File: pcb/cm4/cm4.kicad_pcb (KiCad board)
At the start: 4 copper layers, 100 x 80 mm, 30 parts, among them J101 Conn_02x10_Row_Letter_First, J201 DF40C-100DS-0.4V_51_, J202 DF40C-100DS-0.4V_51_, J301 HR911130A, U201 SN74LV1T34DBV, U301 TPD4EUSB30, U302 TPD4EUSB30, U401 RT9742GGJ5

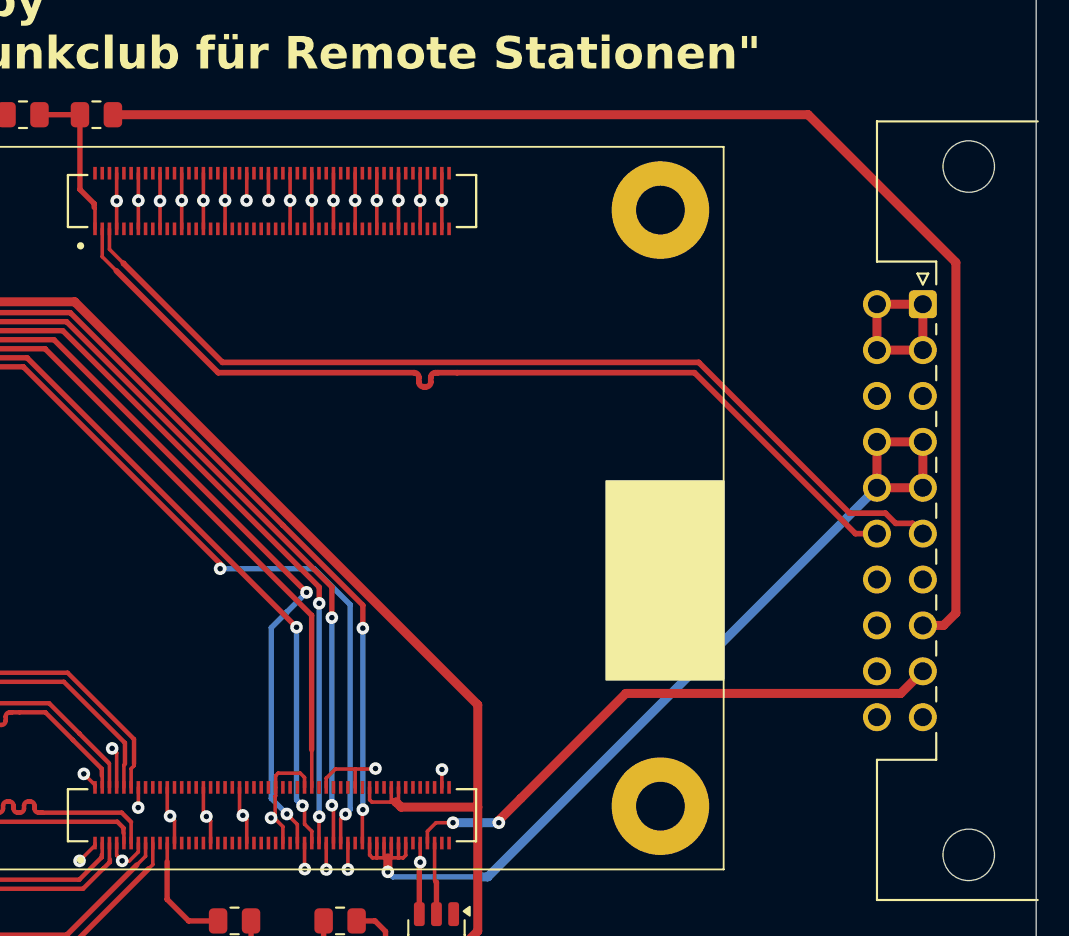
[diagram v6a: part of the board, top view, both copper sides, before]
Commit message: fix pin assignment
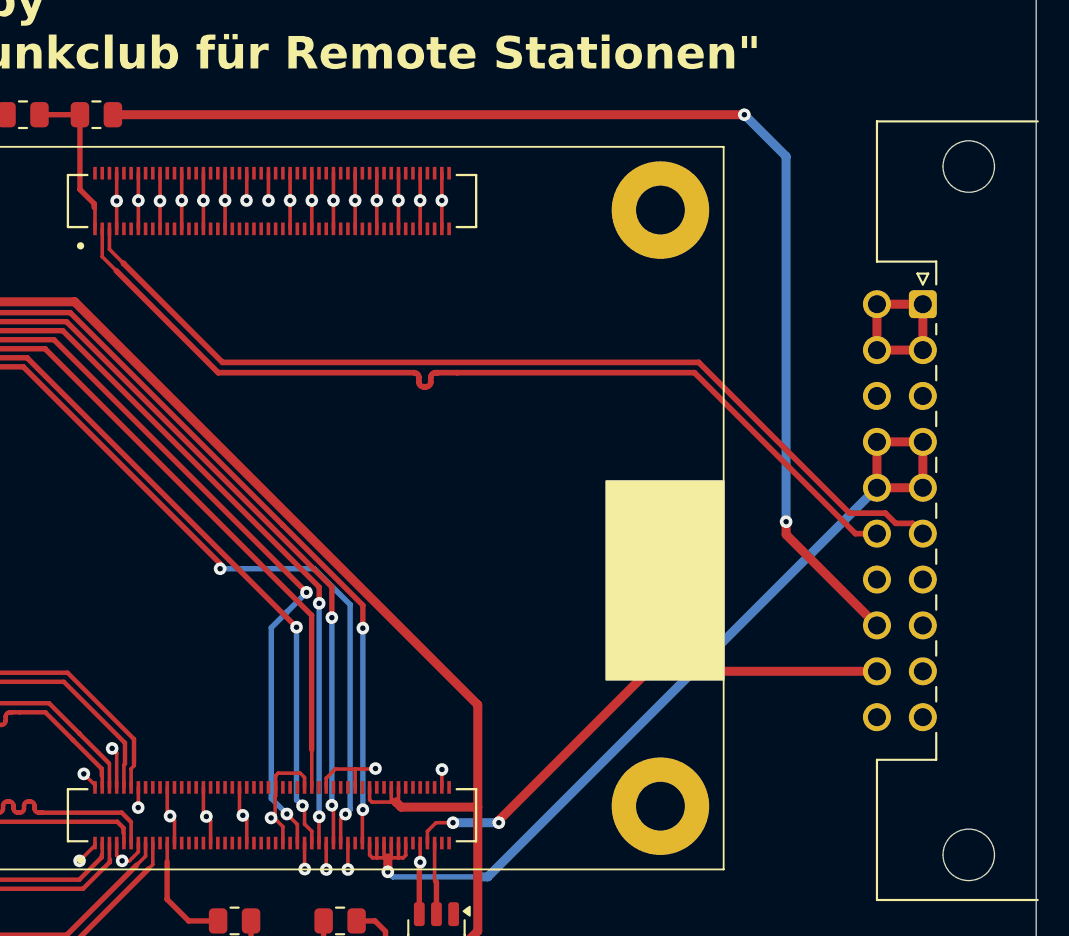
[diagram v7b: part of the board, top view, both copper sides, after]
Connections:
- J101 pad a8: /USB_OTG_ID -> unconnected-(J101-Pin_a8-Pada8)
- J101 pad a9: /nRPIBOOT -> unconnected-(J101-Pin_a9-Pada9)
- J101 pad b8: unconnected-(J101-Pin_b8-Padb8) -> /USB_OTG_ID
- J101 pad b9: unconnected-(J101-Pin_b9-Padb9) -> /nRPIBOOT
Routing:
- net /USB_OTG_ID: track 71.6 -> 66.3 mm, vias 0 -> 2
- net /nRPIBOOT: track 31.8 -> 29.3 mm

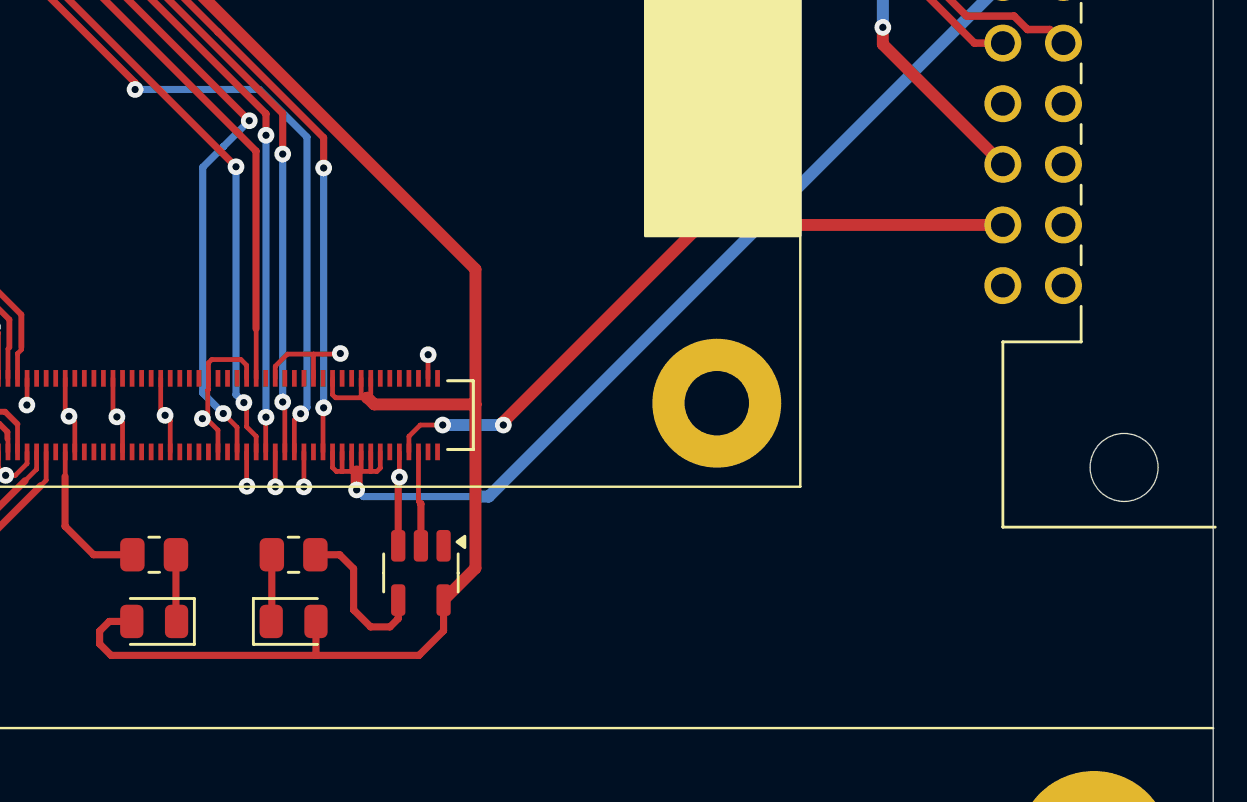
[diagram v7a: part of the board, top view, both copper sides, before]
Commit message: add i2c
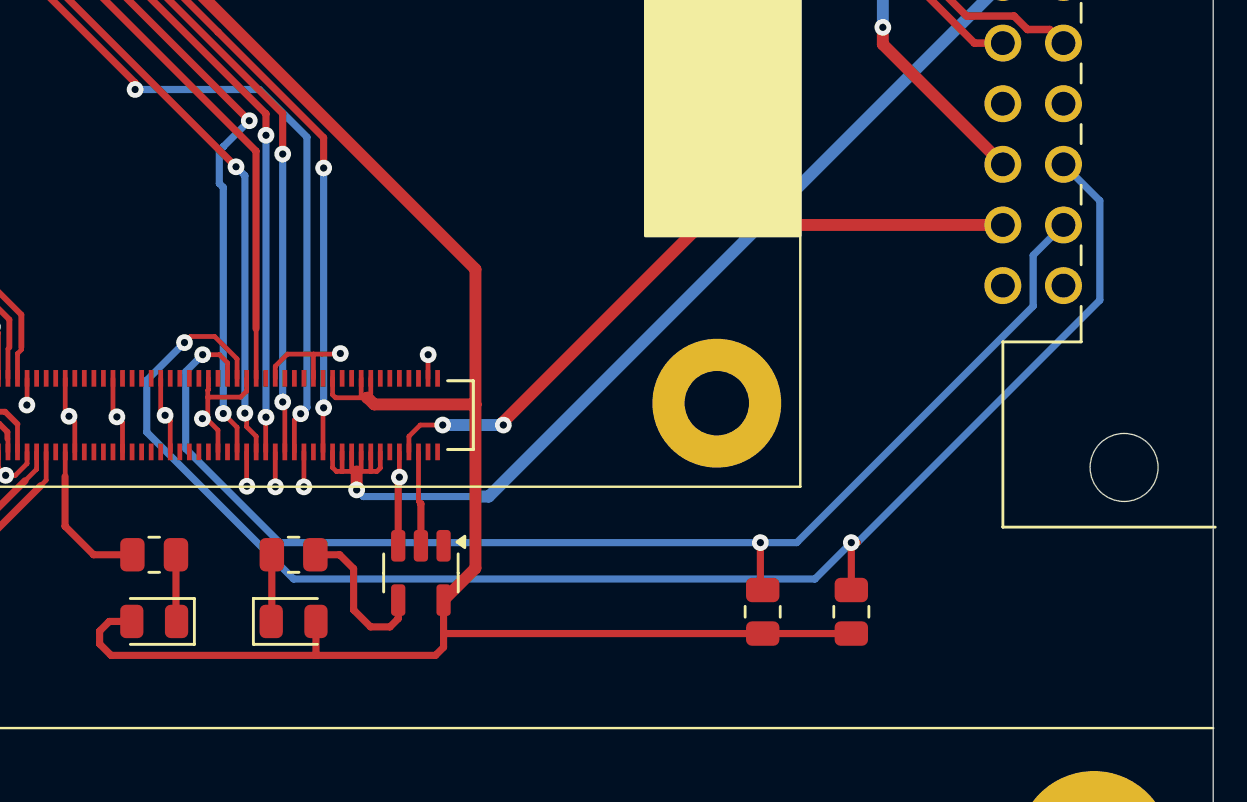
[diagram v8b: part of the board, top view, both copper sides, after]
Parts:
- added R205: 2k2, Resistor_SMD:R_0805_2012Metric, F.Cu at (174.3, 110.9)
- added R206: 2k2, Resistor_SMD:R_0805_2012Metric, F.Cu at (178.1, 110.9)
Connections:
- J101 pad a8: unconnected-(J101-Pin_a8-Pada8) -> /I2C_SDA1
- J101 pad a9: unconnected-(J101-Pin_a9-Pada9) -> /I2C_SCL1
- J201 pad 56: unconnected-(J201-Pad56) -> /I2C_SCL1
- J201 pad 58: unconnected-(J201-Pad58) -> /I2C_SDA1
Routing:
- net /I2C_SDA1: track 0.00 -> 63.6 mm, vias 0 -> 2
- net /I2C_SCL1: track 0.00 -> 53.3 mm, vias 0 -> 2
- net +3V3: track 150.1 -> 167.6 mm
- net GND: track 107.2 -> 106.5 mm
- net /CM4-Board/SD_CLK: track 67.9 -> 67.3 mm
